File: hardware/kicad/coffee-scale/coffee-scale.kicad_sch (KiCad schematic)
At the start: 56 parts, among them J1 Conn_01x08, J2 Conn_01x04, J3 Conn_01x02, J4 USB C, Q1 DMG3415U, Q2 S8550, Q3 BSS138, SW1 SW_Push, SW2 SW_Push, SW3 SW_Push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

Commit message: Update coffee-scale.kicad_sch
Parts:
- C10, C11: footprint (none) -> Capacitor_SMD:C_1206_3216Metric_Pad1.33x1.80mm_HandSolder
- D4: footprint (none) -> Diode_SMD:D_1206_3216Metric_Pad1.42x1.75mm_HandSolder
- H1, H2, H3, H4: footprint (none) -> MountingHole:MountingHole_2.5mm_Pad_TopBottom
- R10: footprint Connector_JST:JST_PH_B2B-PH-K_1x02_P2.00mm_Vertical -> Resistor_SMD:R_1206_3216Metric_Pad1.30x1.75mm_HandSolder
- R11, R12, R13: footprint (none) -> Resistor_SMD:R_1206_3216Metric_Pad1.30x1.75mm_HandSolder
- TP6: footprint (none) -> TestPoint:TestPoint_Pad_1.0x1.0mm
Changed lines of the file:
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@@
 			)
 		)
-		(property "Footprint" ""
+		(property "Footprint" "Resistor_SMD:R_1206_3216Metric_Pad1.30x1.75mm_HandSolder"
 			(at 152.4 78.232 90)
 			(effects
@@
 			)
 		)
-		(property "Footprint" ""
+		(property "Footprint" "MountingHole:MountingHole_2.5mm_Pad_TopBottom"
 			(at 219.71 82.55 0)
 			(effects
@@
 			)
 		)
-		(property "Footprint" ""
+		(property "Footprint" "MountingHole:MountingHole_2.5mm_Pad_TopBottom"
 			(at 219.71 16.51 0)
 			(effects
@@
 			)
 		)
-		(property "Footprint" ""
+		(property "Footprint" "Capacitor_SMD:C_1206_3216Metric_Pad1.33x1.80mm_HandSolder"
 			(at 145.0848 90.17 0)
 			(effects
@@
 			)
 		)
-		(property "Footprint" ""
+		(property "Footprint" "MountingHole:MountingHole_2.5mm_Pad_TopBottom"
 			(at 279.4 16.51 0)
 			(effects
@@
 			)
 		)
-		(property "Footprint" ""
+		(property "Footprint" "Resistor_SMD:R_1206_3216Metric_Pad1.30x1.75mm_HandSolder"
 			(at 248.92 57.912 90)
 			(effects
@@
 			)
 		)
-		(property "Footprint" ""
+		(property "Footprint" "TestPoint:TestPoint_Pad_1.0x1.0mm"
 			(at 22.86 76.2 0)
 			(effects
@@
 			)
 		)
-		(property "Footprint" ""
+		(property "Footprint" "Diode_SMD:D_1206_3216Metric_Pad1.42x1.75mm_HandSolder"
 			(at 259.08 41.91 0)
 			(effects
@@
 			)
 		)
-		(property "Footprint" ""
+		(property "Footprint" "Capacitor_SMD:C_1206_3216Metric_Pad1.33x1.80mm_HandSolder"
 			(at 145.0848 80.01 0)
 			(effects
@@
 			)
 		)
-		(property "Footprint" ""
+		(property "Footprint" "MountingHole:MountingHole_2.5mm_Pad_TopBottom"
 			(at 279.4 82.55 0)
 			(effects
@@
 			)
 		)
-		(property "Footprint" ""
+		(property "Footprint" "Resistor_SMD:R_1206_3216Metric_Pad1.30x1.75mm_HandSolder"
 			(at 152.4 84.328 90)
 			(effects
@@
 			)
 		)
-		(property "Footprint" "Connector_JST:JST_PH_B2B-PH-K_1x02_P2.00mm_Vertical"
+		(property "Footprint" "Resistor_SMD:R_1206_3216Metric_Pad1.30x1.75mm_HandSolder"
 			(at 29.21 170.18 0)
 			(effects

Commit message: PCB Update
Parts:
- D4: footprint Diode_SMD:D_1206_3216Metric_Pad1.42x1.75mm_HandSolder -> Diode_SMD:D_SOD-123
- J3: footprint Connector_JST:JST_PH_B2B-PH-K_1x02_P2.00mm_Vertical -> Connector_JST:JST_PH_S2B-PH-K_1x02_P2.00mm_Horizontal
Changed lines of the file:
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@@
 			)
 		)
-		(property "Footprint" "Connector_JST:JST_PH_B2B-PH-K_1x02_P2.00mm_Vertical"
+		(property "Footprint" "Connector_JST:JST_PH_S2B-PH-K_1x02_P2.00mm_Horizontal"
 			(at 21.59 176.53 0)
 			(effects
@@
 			)
 		)
-		(property "Footprint" "Diode_SMD:D_1206_3216Metric_Pad1.42x1.75mm_HandSolder"
+		(property "Footprint" "Diode_SMD:D_SOD-123"
 			(at 259.08 41.91 0)
 			(effects

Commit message: Update schematic
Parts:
- D1: value MBR540 -> ~; footprint Diode_THT:D_DO-201AD_P15.24mm_Horizontal -> Diode_SMD:D_SOD-128
- Q2: footprint Package_TO_SOT_THT:TO-92_Inline -> Package_TO_SOT_SMD:SOT-23-3
- U4: footprint Package_TO_SOT_SMD:SOT-23-5 -> Package_TO_SOT_SMD:SOT-89-5_Handsoldering
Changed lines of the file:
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@@
 			)
 		)
-		(property "Footprint" "Package_TO_SOT_SMD:SOT-23-5"
+		(property "Footprint" "Package_TO_SOT_SMD:SOT-89-5_Handsoldering"
 			(at 110.998 149.098 0)
 			(effects
@@
 			)
 		)
-		(property "Footprint" "Package_TO_SOT_THT:TO-92_Inline"
+		(property "Footprint" "Package_TO_SOT_SMD:SOT-23-3"
 			(at 73.66 33.655 0)
 			(effects
@@
 			)
 		)
-		(property "Value" "MBR540"
+		(property "Value" "~"
 			(at 77.724 171.196 0)
 			(effects
@@
 			)
 		)
-		(property "Footprint" "Diode_THT:D_DO-201AD_P15.24mm_Horizontal"
+		(property "Footprint" "Diode_SMD:D_SOD-128"
 			(at 77.47 169.545 0)
 			(effects

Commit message: Update footprints
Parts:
- D1: MPN (none) -> PMEG4050EP,115
- D4: footprint Diode_SMD:D_SOD-123 -> Diode_SMD:D_SOD-128; MPN (none) -> DMG2301L-7
- J4: MPN (none) -> USB4085-GF-A
- Q1: MPN (none) -> DMG2301L-7
- Q2: MPN (none) -> S8550
- Q3: MPN (none) -> BSS138
- U1: MPN (none) -> ESP32-S3-WROOM-1-N16
- U2: MPN (none) -> HX711
- U4: MPN (none) -> AP2112R5-3.3TRG1
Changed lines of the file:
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@@
 			)
 		)
+		(property "MPN" "AP2112R5-3.3TRG1"
+			(at 113.03 176.53 0)
+			(effects
+				(font
+					(size 1.27 1.27)
+				)
+				(hide yes)
+			)
+		)
 		(pin "1"
 		)
@@
 			)
 		)
+		(property "MPN" "DMG2301L-7"
+			(at 81.28 167.64 0)
+			(effects
+				(font
+					(size 1.27 1.27)
+				)
+				(hide yes)
+			)
+		)
 		(pin "2"
 		)
@@
 			)
 		)
+		(property "MPN" "BSS138"
+			(at 261.62 59.69 0)
+			(effects
+				(font
+					(size 1.27 1.27)
+				)
+				(hide yes)
+			)
+		)
 		(pin "3"
 		)
@@
 			)
 		)
+		(property "MPN" "ESP32-S3-WROOM-1-N16"
+			(at 179.07 67.31 0)
+			(effects
+				(font
+					(size 1.27 1.27)
+				)
+				(hide yes)
+			)
+		)
 		(pin "8"
 		)
@@
 			)
 		)
+		(property "MPN" "S8550"
+			(at 78.74 35.56 0)
+			(effects
+				(font
+					(size 1.27 1.27)
+				)
+				(hide yes)
+			)
+		)
 		(pin "3"
 		)
@@
 			)
 		)
+		(property "MPN" "PMEG4050EP,115"
+			(at 77.47 173.99 0)
+			(effects
+				(font
+					(size 1.27 1.27)
+				)
+				(hide yes)
+			)
+		)
 		(pin "2"
 		)
@@
 			)
 		)
-		(property "Footprint" "Diode_SMD:D_SOD-123"
+		(property "Footprint" "Diode_SMD:D_SOD-128"
 			(at 259.08 41.91 0)
 			(effects
@@
 			)
 		)
+		(property "MPN" "DMG2301L-7 "
+			(at 259.08 41.91 90)
+			(effects
+				(font
+					(size 1.27 1.27)
+				)
+				(hide yes)
+			)
+		)
 		(pin "1"
 		)
@@
 			)
 		)
+		(property "MPN" "USB4085-GF-A"
+			(at 25.4 116.84 0)
+			(effects
+				(font
+					(size 1.27 1.27)
+				)
+				(hide yes)
+			)
+		)
 		(pin "S1"
 		)
@@
 			(effects
 				(font
+					(size 1.27 1.27)
+				)
+				(hide yes)
+			)
+		)
+		(property "MPN" "HX711"
+			(at 113.03 50.8 0)
+			(effects
+				(font

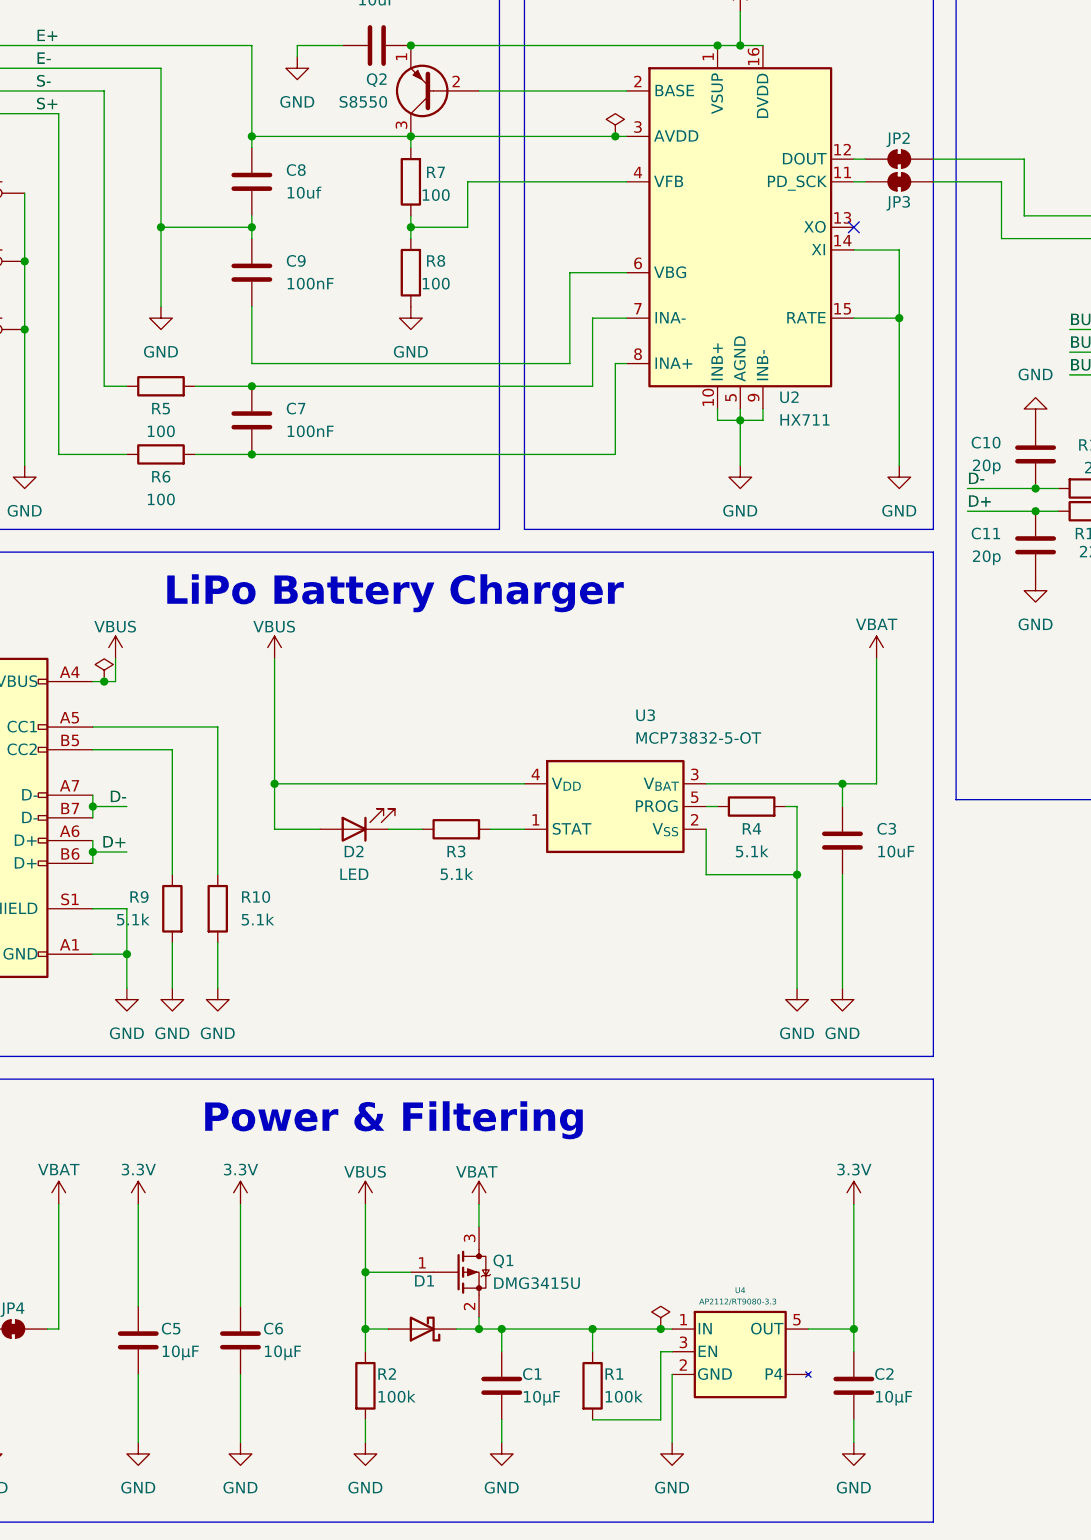
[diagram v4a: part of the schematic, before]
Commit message: Update footprints
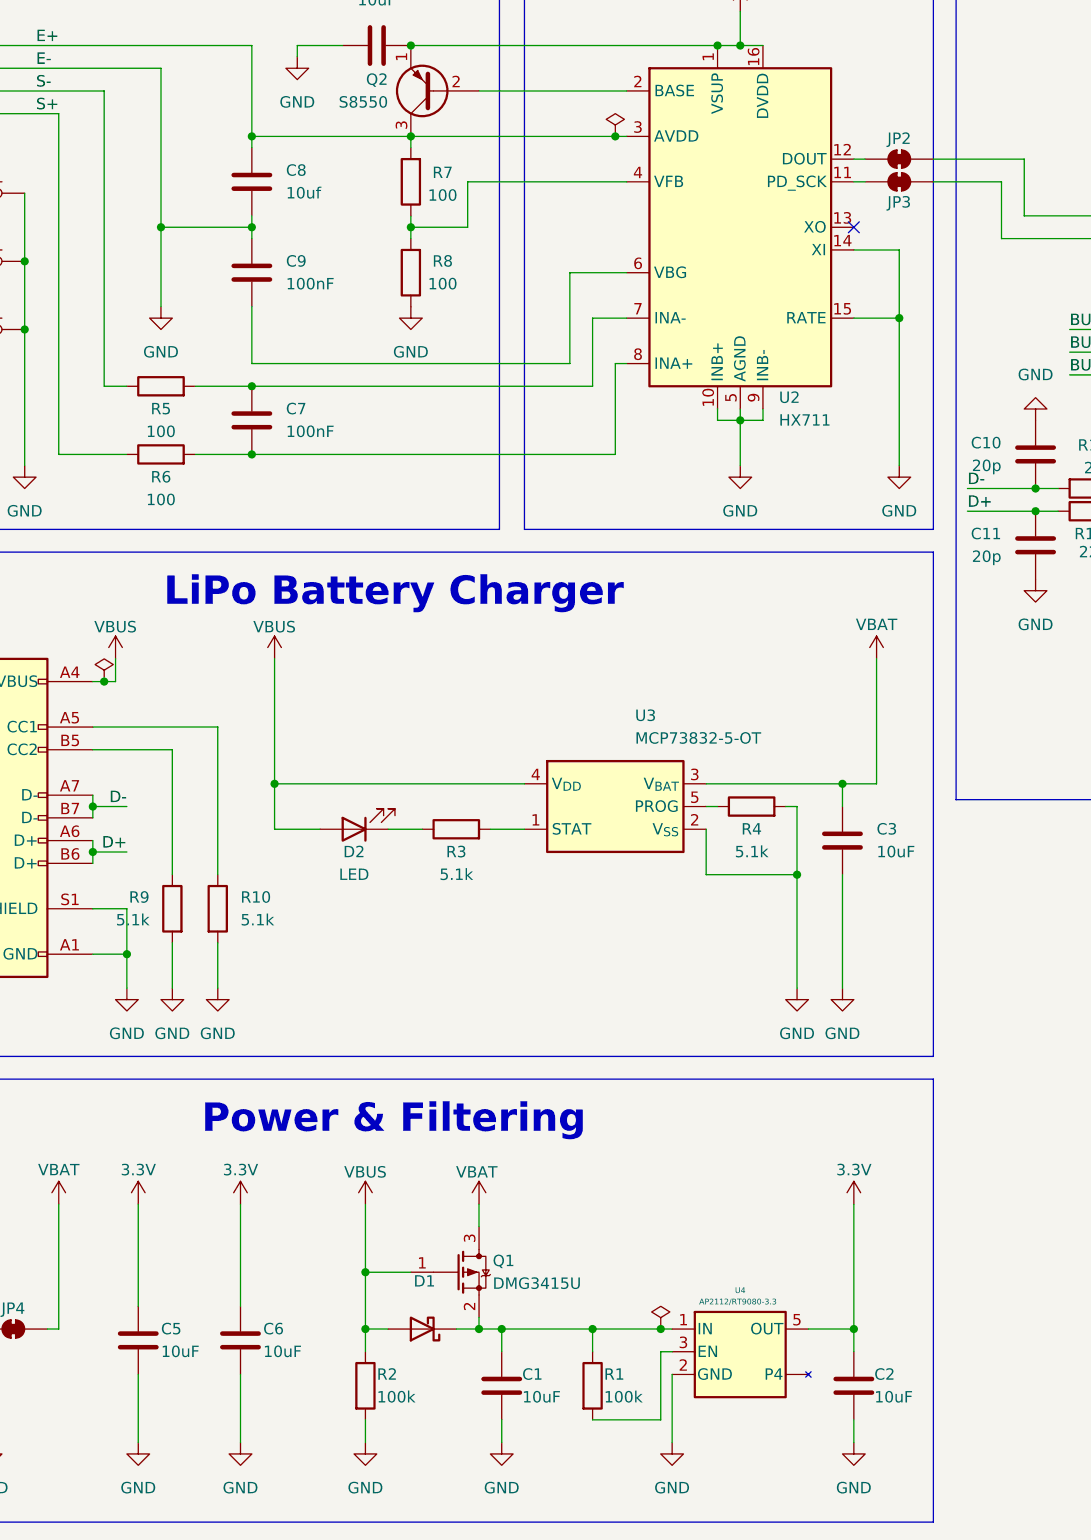
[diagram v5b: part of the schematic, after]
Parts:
- C1, C2, C5, C6: value 10μF -> 10uF
- SW1, SW2: footprint Button_Switch_SMD:SW_SPST_Omron_B3FS-105xP -> Button_Switch_SMD:SW_SPST_B3S-1000
- SW3: footprint Button_Switch_SMD:SW_SPST_Omron_B3FS-105xP -> Button_Switch_SMD:SW_SPST_B3S-1100
- U3: MPN (none) -> MCP73832T-5ACI/OT
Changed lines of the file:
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@@
 			)
 		)
-		(property "Footprint" "Button_Switch_SMD:SW_SPST_Omron_B3FS-105xP"
+		(property "Footprint" "Button_Switch_SMD:SW_SPST_B3S-1100"
 			(at 27.94 57.15 0)
 			(effects
@@
 			)
 		)
+		(property "MPN" "MCP73832T-5ACI/OT"
+			(at 99.06 115.57 0)
+			(effects
+				(font
+					(size 1.27 1.27)
+				)
+				(hide yes)
+			)
+		)
 		(pin "1"
 		)
@@
 		(dnp no)
 		(property "Reference" "R8"
-			(at 78.994 54.61 0)
+			(at 79.756 54.61 0)
 			(effects
 				(font
@@
 		)
 		(property "Value" "100"
-			(at 78.994 57.15 0)
+			(at 79.756 57.15 0)
 			(effects
 				(font
@@
 			)
 		)
-		(property "Footprint" "Button_Switch_SMD:SW_SPST_Omron_B3FS-105xP"
+		(property "Footprint" "Button_Switch_SMD:SW_SPST_B3S-1000"
 			(at 27.94 49.53 0)
 			(effects
@@
 			)
 		)
-		(property "Value" "10μF"
+		(property "Value" "10uF"
 			(at 48.26 176.53 0)
 			(effects
@@
 			)
 		)
-		(property "Value" "10μF"
+		(property "Value" "10uF"
 			(at 88.646 181.61 0)
 			(effects
@@
 			)
 		)
-		(property "Value" "10μF"
+		(property "Value" "10uF"
 			(at 59.69 176.53 0)
 			(effects
@@
 			)
 		)
-		(property "Value" "10μF"
+		(property "Value" "10uF"
 			(at 128.016 181.61 0)
 			(effects
@@
 		(dnp no)
 		(property "Reference" "R7"
-			(at 78.994 44.704 0)
+			(at 79.756 44.704 0)
 			(effects
 				(font
@@
 		)
 		(property "Value" "100"
-			(at 78.994 47.244 0)
+			(at 79.756 47.244 0)
 			(effects
 				(font
@@
 			)
 		)
-		(property "Footprint" "Button_Switch_SMD:SW_SPST_Omron_B3FS-105xP"
+		(property "Footprint" "Button_Switch_SMD:SW_SPST_B3S-1000"
 			(at 27.94 41.91 0)
 			(effects
